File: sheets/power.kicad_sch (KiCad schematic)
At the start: 36 parts, among them J2 USB_C_Receptacle_USB2.0_16P, SW3 SW_SPDT, SW4 SW_SPST, U2 USBLC6-2P6, U3 TPS54620RGYR, U4 AMS1117-3.3, U5 LMR51430XFDDCR

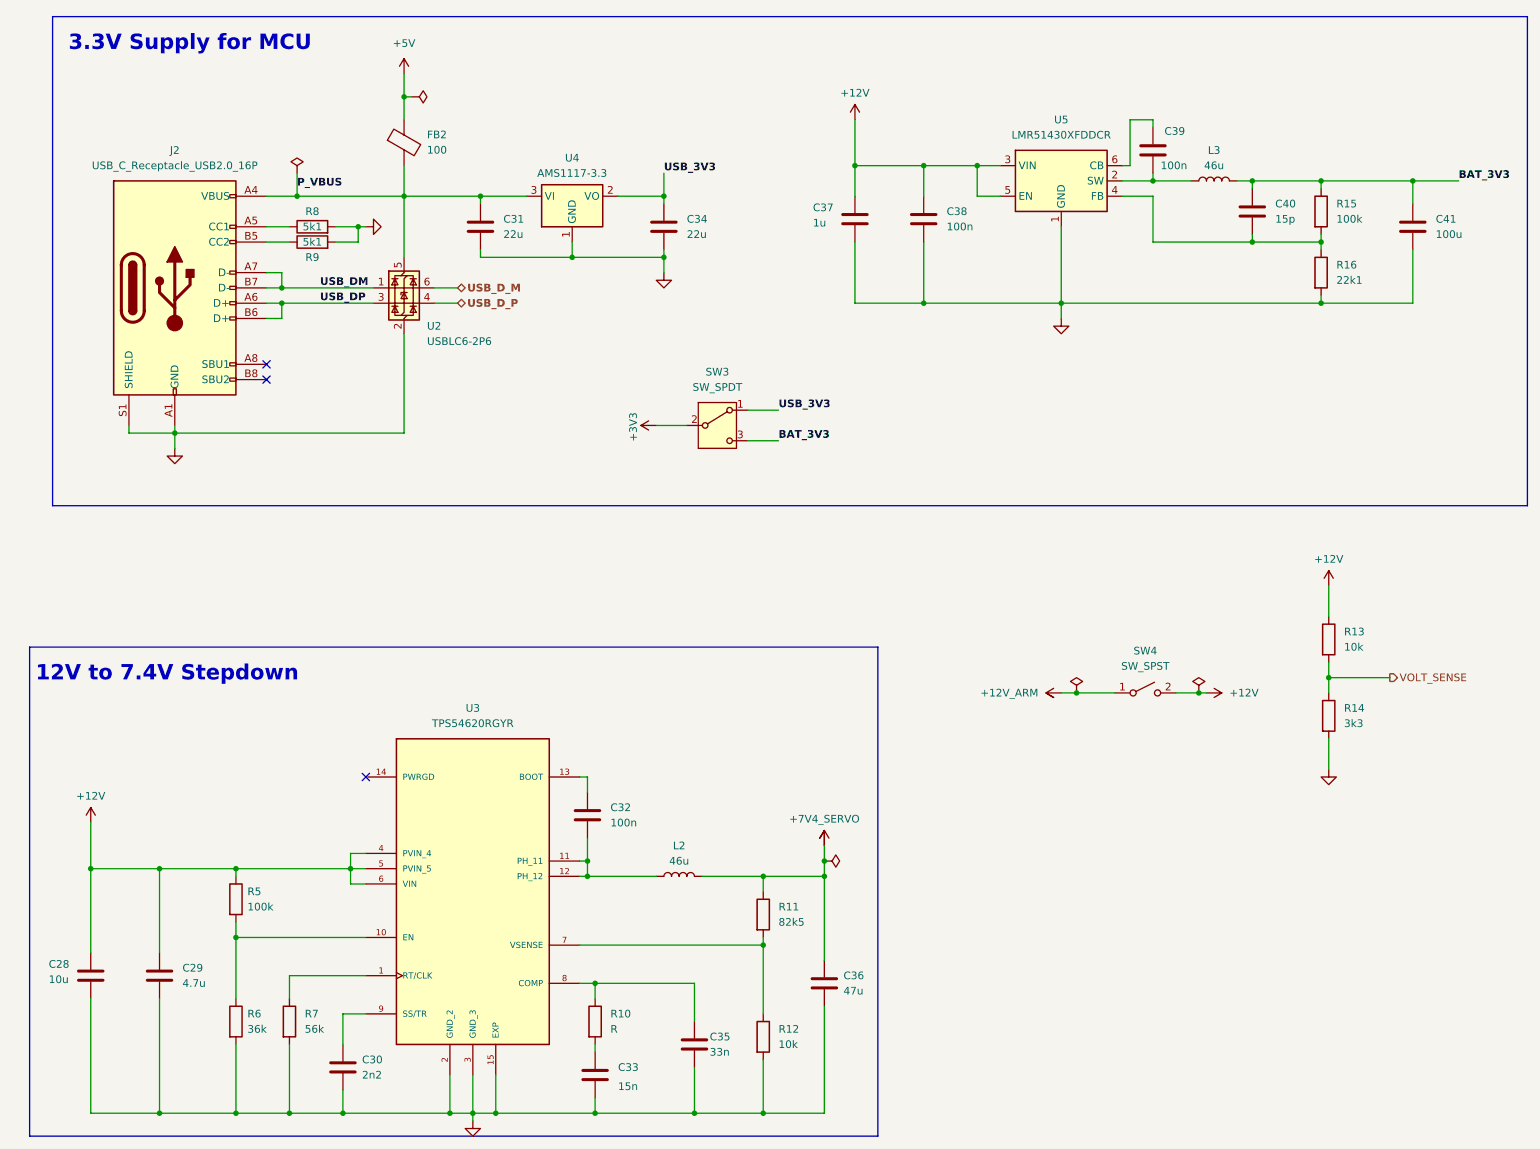
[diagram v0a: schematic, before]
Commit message: solved reverse polarity w pmos and tvs clamp
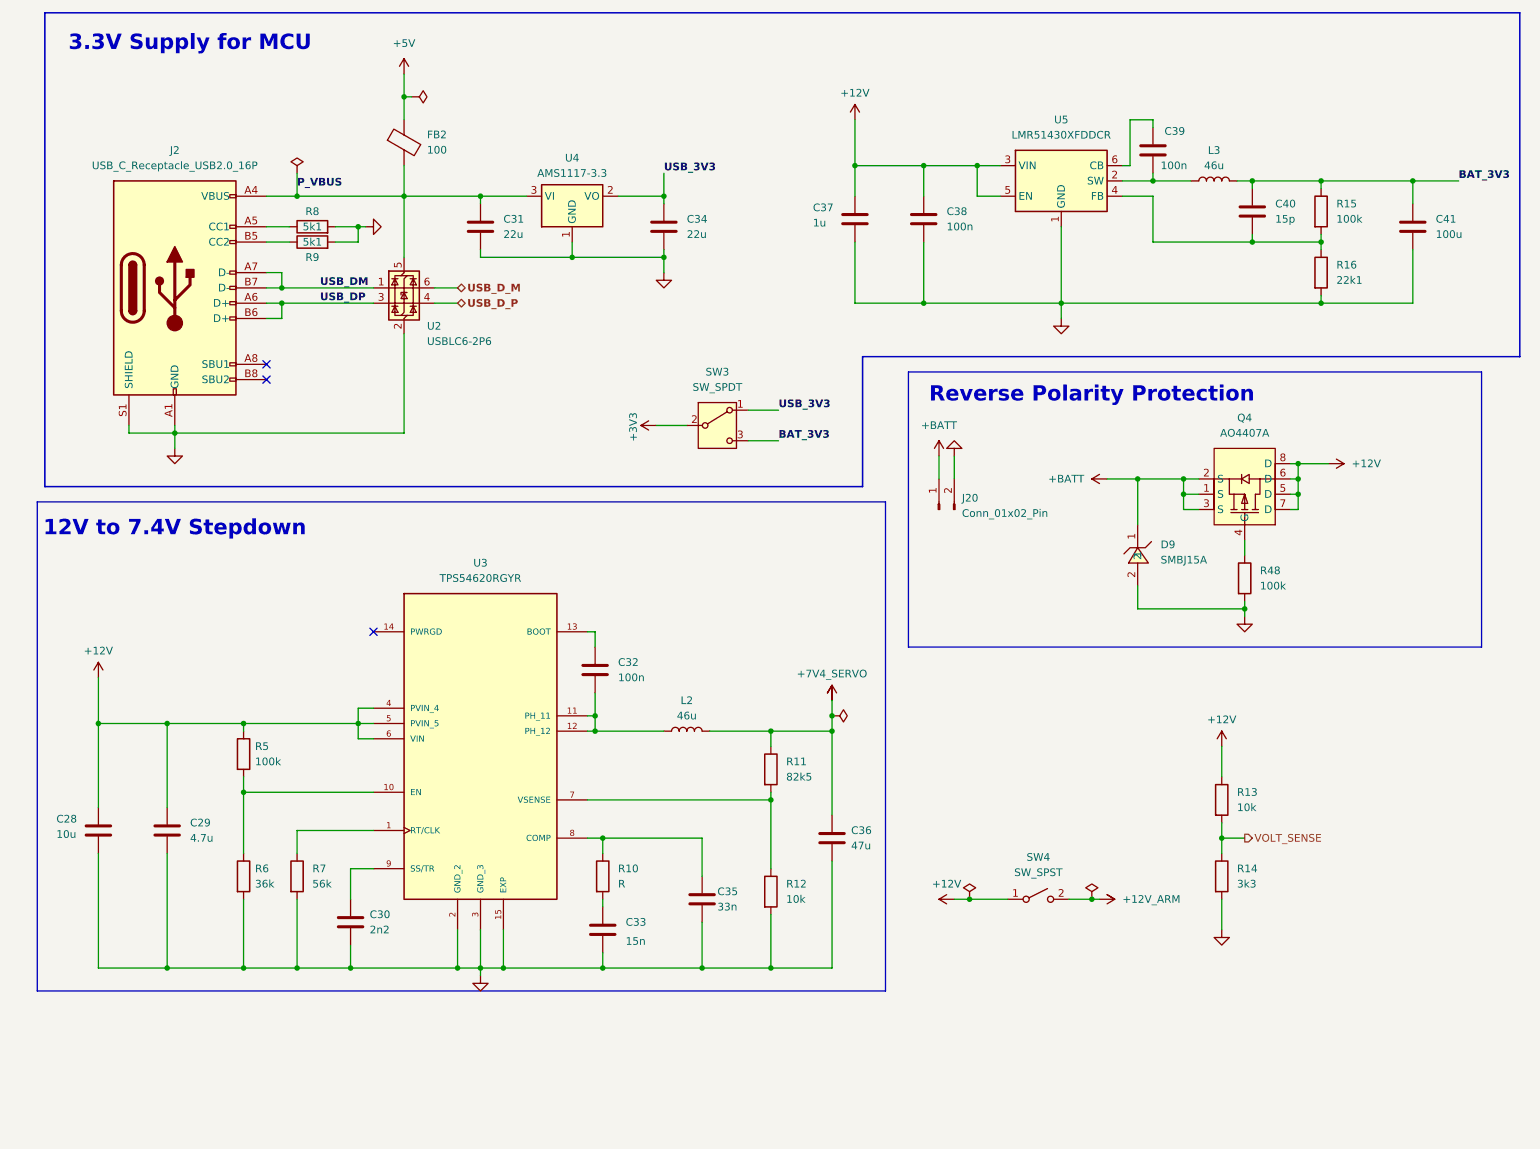
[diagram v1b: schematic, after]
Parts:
- added D9: SMBJ15A, aerolotl_custom:SMB_L4.6-W3.6-LS5.3-RD, symbol aerolotl_custom:SMBJ15A_C83846
- added J20: Conn_01x02_Pin, symbol Connector:Conn_01x02_Pin
- added Q4: AO4407A, aerolotl_custom:SOIC-8_L4.9-W3.9-P1.27-LS6.0-BL, symbol aerolotl_custom:AO4407A
- added R48: 100k, symbol Device:R
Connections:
- net +12V: now also SW4.1 (A), Q4.5 (D), Q4.6 (D), Q4.7 (D), Q4.8 (D); no longer SW4.2 (B)
- net +12V_ARM: now also SW4.2 (B); no longer SW4.1 (A)
- net GND: now also D9.2, J20.2 (Pin_2), R48.2
- new net: Q4.4 (G), R48.1
- new net +BATT: D9.1, J20.1 (Pin_1), Q4.1 (S), Q4.2 (S), Q4.3 (S)
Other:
- note added: "Reverse Polarity Protection"
- moved on the sheet: C28, C29, C30, C32, C33, C35, C36, L2, R10, R11, R12, R13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
